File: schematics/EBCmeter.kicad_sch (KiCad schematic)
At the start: 27 parts, among them Q1 BSS214NH, Q2 BSS214NH, Q3 BSS214NH, Q4 BSS214NH, U1 PIC16F15325-DIP, U2 AD8615AUJZ-R2, U3 LM4040DBZ-2.0, U4 TSZ122IDT, U5 LM4040

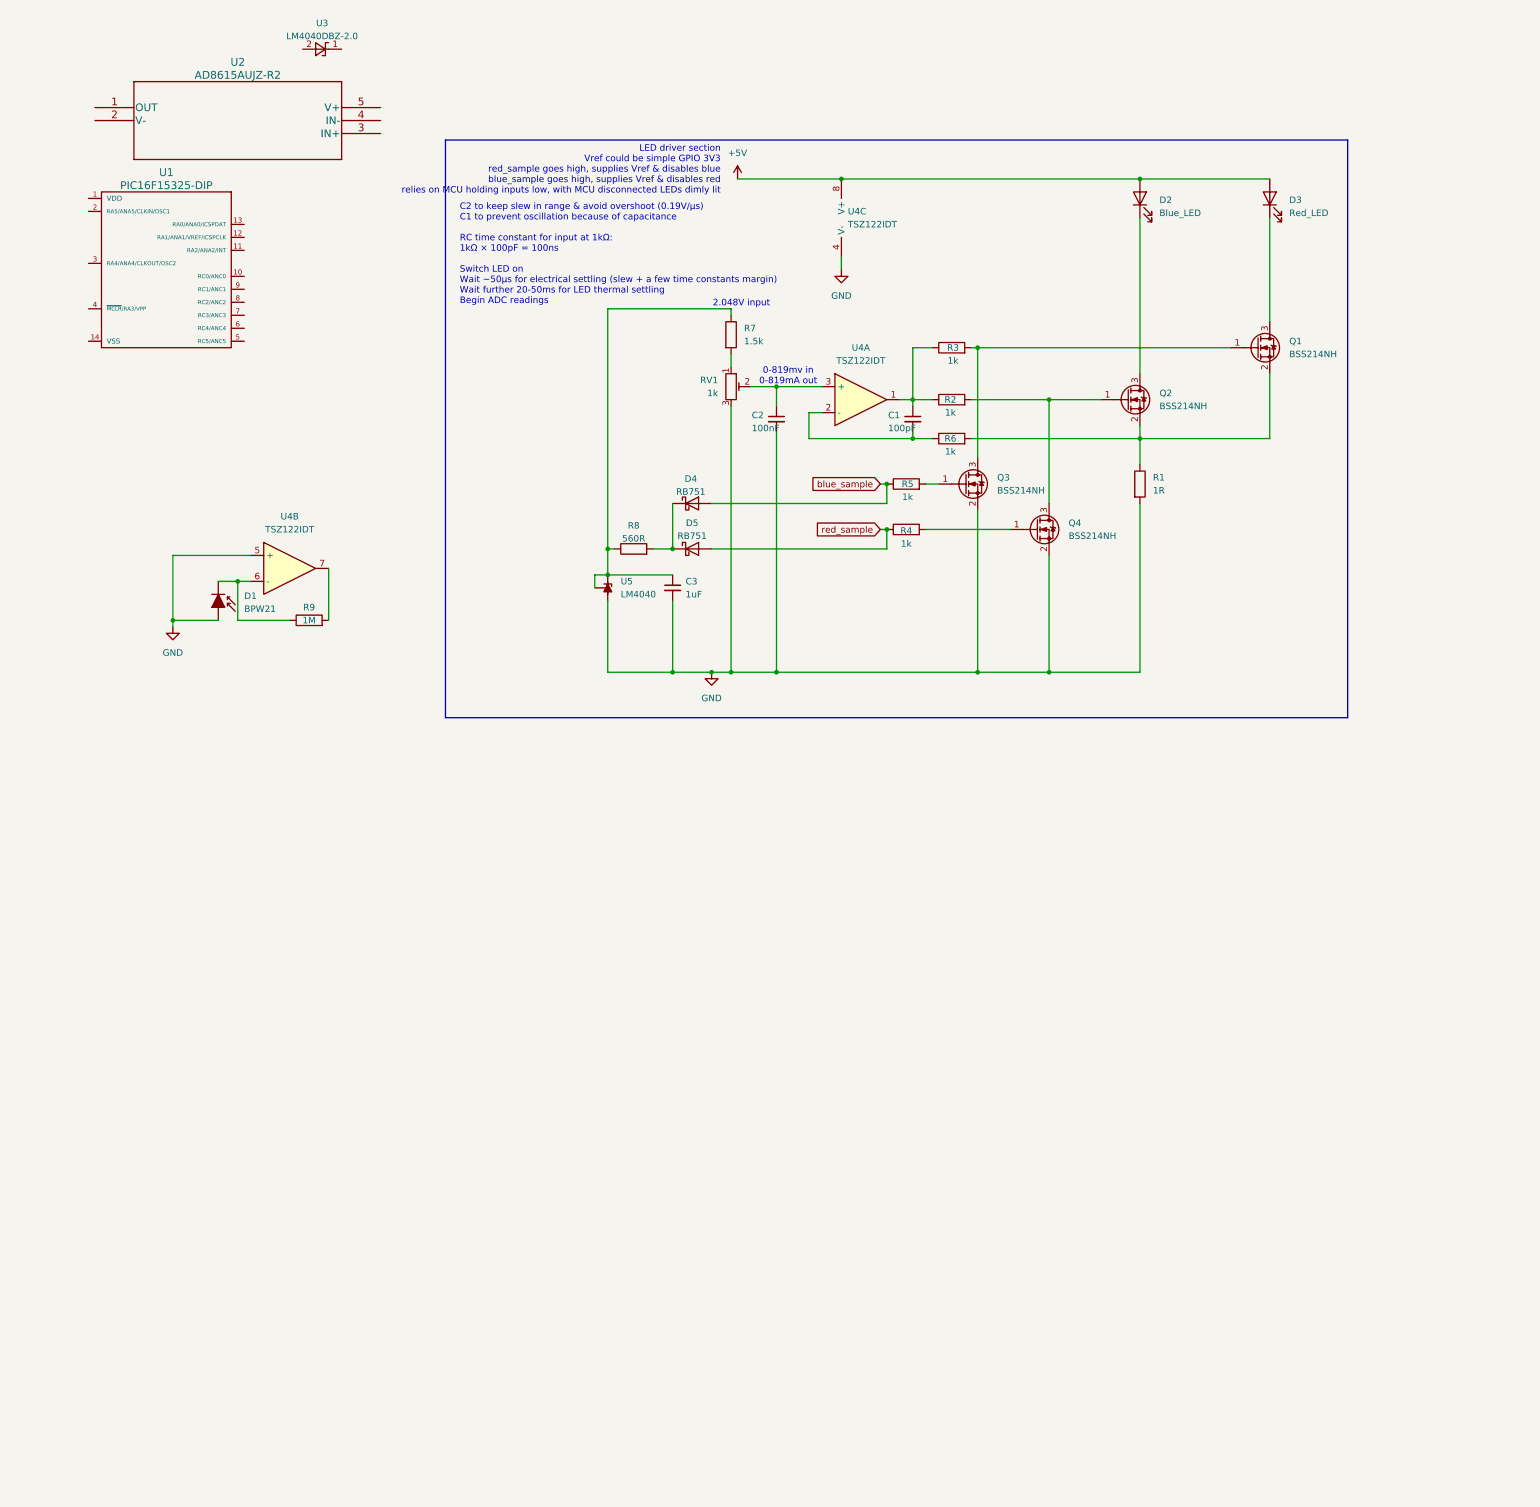
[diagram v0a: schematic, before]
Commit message: updated schematic
Added in power supply rails & voltage references
Added switchable gain, ADC
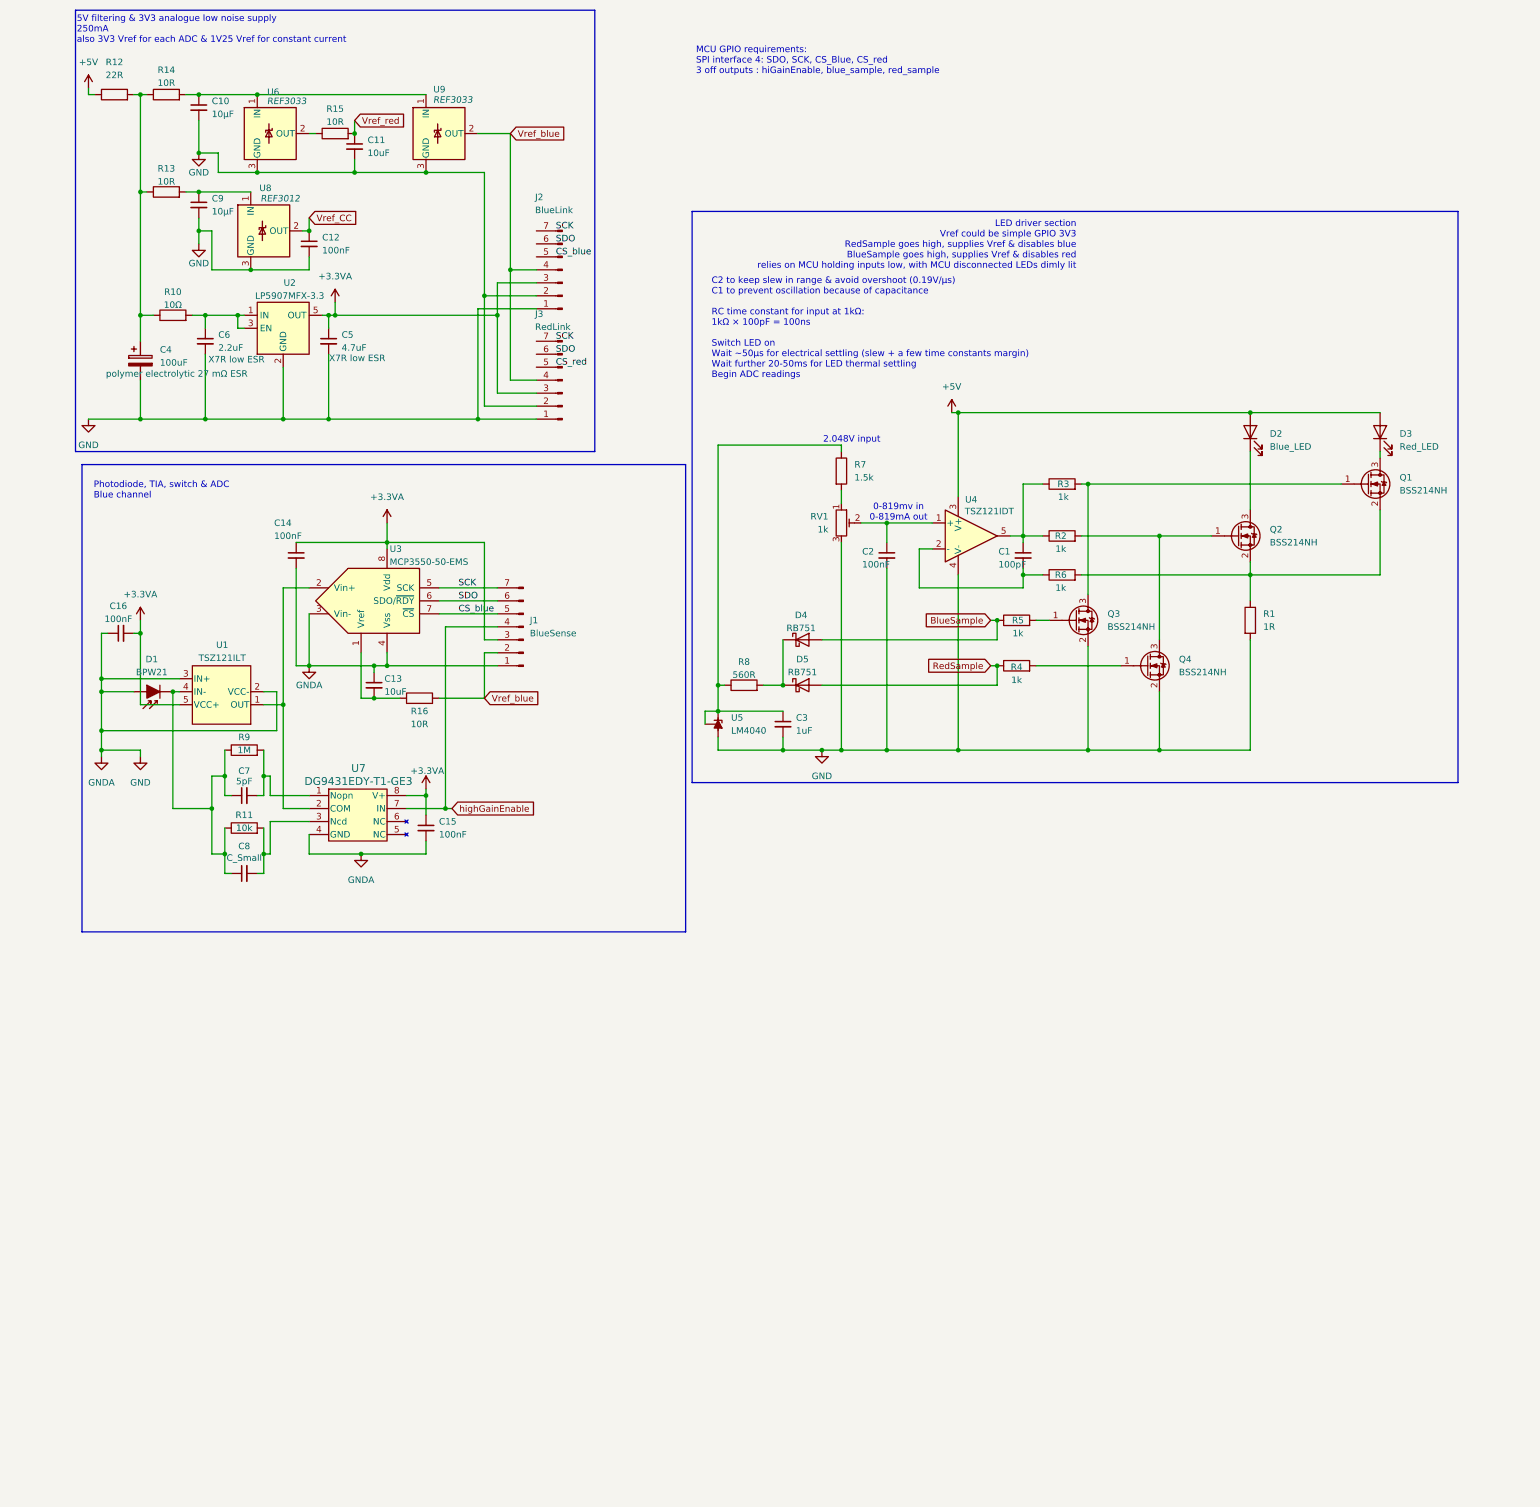
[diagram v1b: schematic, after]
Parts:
- removed U1: PIC16F15325-DIP, symbol w_microcontrollers:PIC16F15325-DIP
- removed U2: AD8615AUJZ-R2, UJ_5_ADI, symbol AD8615AUJZ-R2:AD8615AUJZ-R2
- removed U3: LM4040DBZ-2.0, Package_TO_SOT_SMD:SOT-23, symbol Reference_Voltage:LM4040DBZ-2.0
- removed unit 3 of U4
- removed unit 2 of U4
- added C10, C9: 10µF, symbol Device:C_Small
- added C11, C13: 10uF, symbol Device:C_Small
- added C12, C14, C15, C16: 100nF, symbol Device:C_Small
- added C4: 100uF, symbol Device:C_Polarized
- added C5: 4.7uF, symbol Device:C_Small
- added C6: 2.2uF, symbol Device:C_Small
- added C7: 5pF, symbol Device:C_Small
- added C8: C_Small, symbol Device:C_Small
- added J1: BlueSense, symbol Connector:Conn_01x07_Pin
- added J2: BlueLink, symbol Connector:Conn_01x07_Pin
- added J3: RedLink, symbol Connector:Conn_01x07_Pin
- added R10: 10Ω, symbol Device:R
- added R11: 10k, symbol Device:R
- added R12: 22R, symbol Device:R
- added R13, R14, R15, R16: 10R, symbol Device:R
- added U1: TSZ121ILT, SOT23-5_STM, symbol Personal_Library:TSZ121ILT
- added U2: LP5907MFX-3.3, Package_TO_SOT_SMD:SOT-23-5, symbol Regulator_Linear:LP5907MFX-3.3
- added U3: MCP3550-50-EMS, symbol Analog_ADC:MCP3550-50-EMS
- added U6, U9: REF3033, Package_TO_SOT_SMD:SOT-23, symbol Reference_Voltage:REF3033
- added U7: DG9431EDY-T1-GE3, SOIC_DG9431EDY-T1-GE3_VIS, symbol Personal_Library:DG9431EDY-T1-GE3
- added U8: REF3012, Package_TO_SOT_SMD:SOT-23, symbol Reference_Voltage:REF3012
- U4: value TSZ122IDT -> TSZ121IDT; symbol Device:Opamp_Dual -> Simulation_SPICE:OPAMP
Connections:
- net +5V: now also U4.3 (V+), R12.1
- net GND: now also U4.4 (V-), C10.2, C11.2, C12.2, C13.1, C14.2, C15.2, C16.1, C4.2, C5.2, C6.2, C9.2, J1.1 (Pin_1), J2.1 (Pin_1), J2.2 (Pin_2), J3.1 (Pin_1), J3.2 (Pin_2), U1.2 (VCC-), U1.3 (IN+), U2.2 (GND), U3.3 (Vin-), U3.4 (Vss), U6.3 (GND), U7.4 (GND), U8.3 (GND), U9.3 (GND)
- net at C1.1, R2.1, R3.1: now also U4.5; no longer U4.1
- net at C2.1, RV1.2: now also U4.1 (+); no longer U4.3 (+)
- net at D1.1 (K), R9.1: now also C7.1, C8.1, R11.1, U1.4 (IN-)
- net at R9.2: now also C7.2, U7.1 (Nopn)
- net blue_sample renamed BlueSample
- net red_sample renamed RedSample
- new net: C6.1, R10.2, U2.1 (IN), U2.3 (EN)
- new net: C10.1, R14.2, U6.1 (IN), U9.1 (IN)
- new net: C4.1, R10.1, R12.2, R13.1, R14.1
- new net: C8.2, R11.2, U7.3 (Ncd)
- new net: C13.2, R16.1, U3.1 (Vref)
- new net: U1.1 (OUT), U3.2 (Vin+), U7.2 (COM)
- new net: R15.1, U6.2 (OUT)
- new net: C9.1, R13.2, U8.1 (IN)
- new net +3.3VA: C14.1, C15.1, C16.2, C5.1, J1.3 (Pin_3), J2.3 (Pin_3), J3.3 (Pin_3), U1.5 (VCC+), U2.5 (OUT), U3.8 (Vdd), U7.8 (V+)
- new net CS_blue: J1.5 (Pin_5), U3.7 (~{CS})
- new net SCK: J1.7 (Pin_7), U3.5 (SCK)
- new net SDO: J1.6 (Pin_6), U3.6 (SDO/~{RDY})
- new net Vref_CC: C12.1, U8.2 (OUT)
- new net Vref_blue: J1.2 (Pin_2), J2.4 (Pin_4), J3.4 (Pin_4), R16.2, U9.2 (OUT)
- new net Vref_red: C11.1, R15.2
- new net highGainEnable: J1.4 (Pin_4), U7.7 (IN)
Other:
- note added: "5V filtering & 3V3 analogue low noise supply 250mA also 3V3 Vref for each ADC & 1V25 Vref for constant current"
- note added: "LED driver section Vref could be simple GPIO 3V3 RedSample goes high, supplies Vref & disables blue BlueSample goes high, supplies Vref & disables red relies on MCU holding inputs low, with MCU disconnected LEDs dimly lit"
- note added: "MCU GPIO requirements: SPI interface 4: SDO, SCK, CS_Blue, CS_red 3 off outputs : hiGainEnable, blue_sample, red_sample"
- note added: "Photodiode, TIA, switch & ADC Blue channel"
- note removed: "LED driver section Vref could be simple GPIO 3V3 red_sample goes high, supplies Vref & disables blue blue_sample goes high, supplies Vref & disables red relies on MCU holding inputs low, with MCU disconnected LEDs dimly lit"
- moved on the sheet: C1, C2, C3, D1, D2, D3, D4, D5, Q1, Q2, Q3, Q4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
